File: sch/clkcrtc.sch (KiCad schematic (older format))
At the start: 26 parts, among them Q1 16 MHz, Q2 13.333 MHz

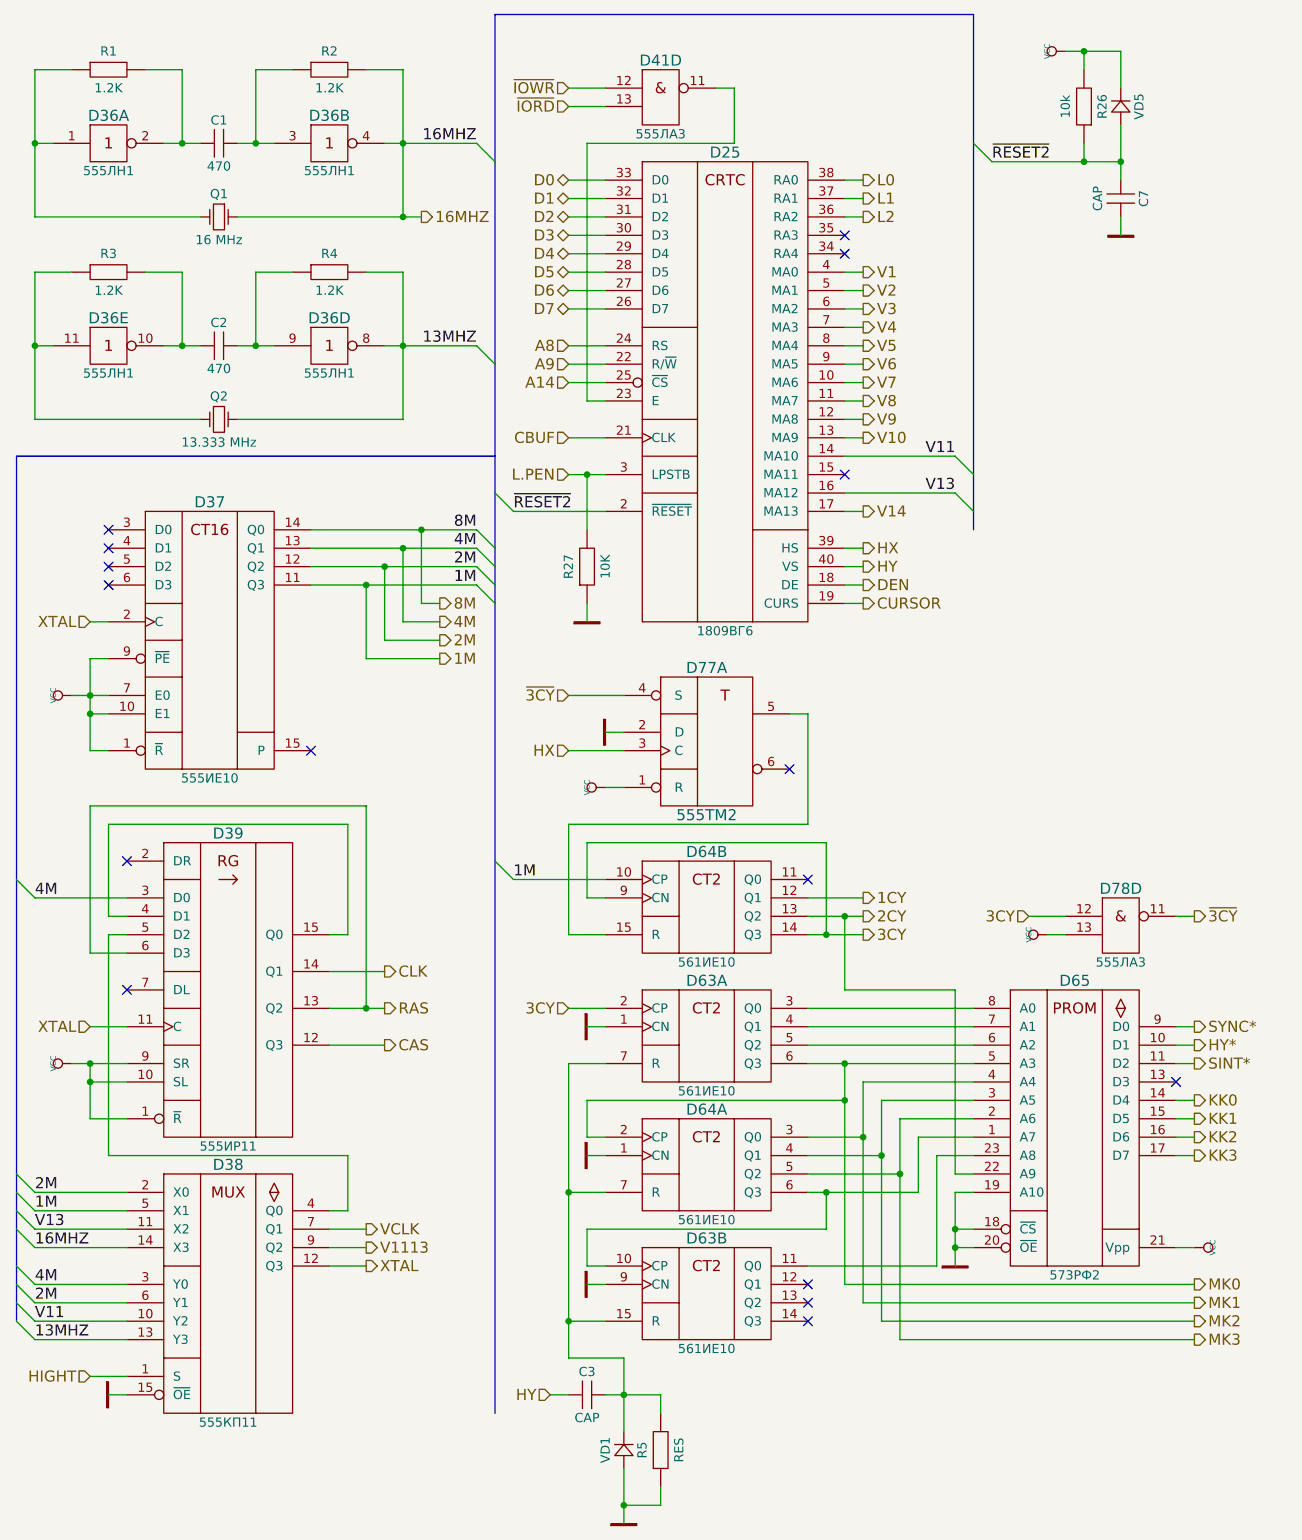
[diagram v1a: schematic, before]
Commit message: IR22 and IR23 symbols updated, part values updated
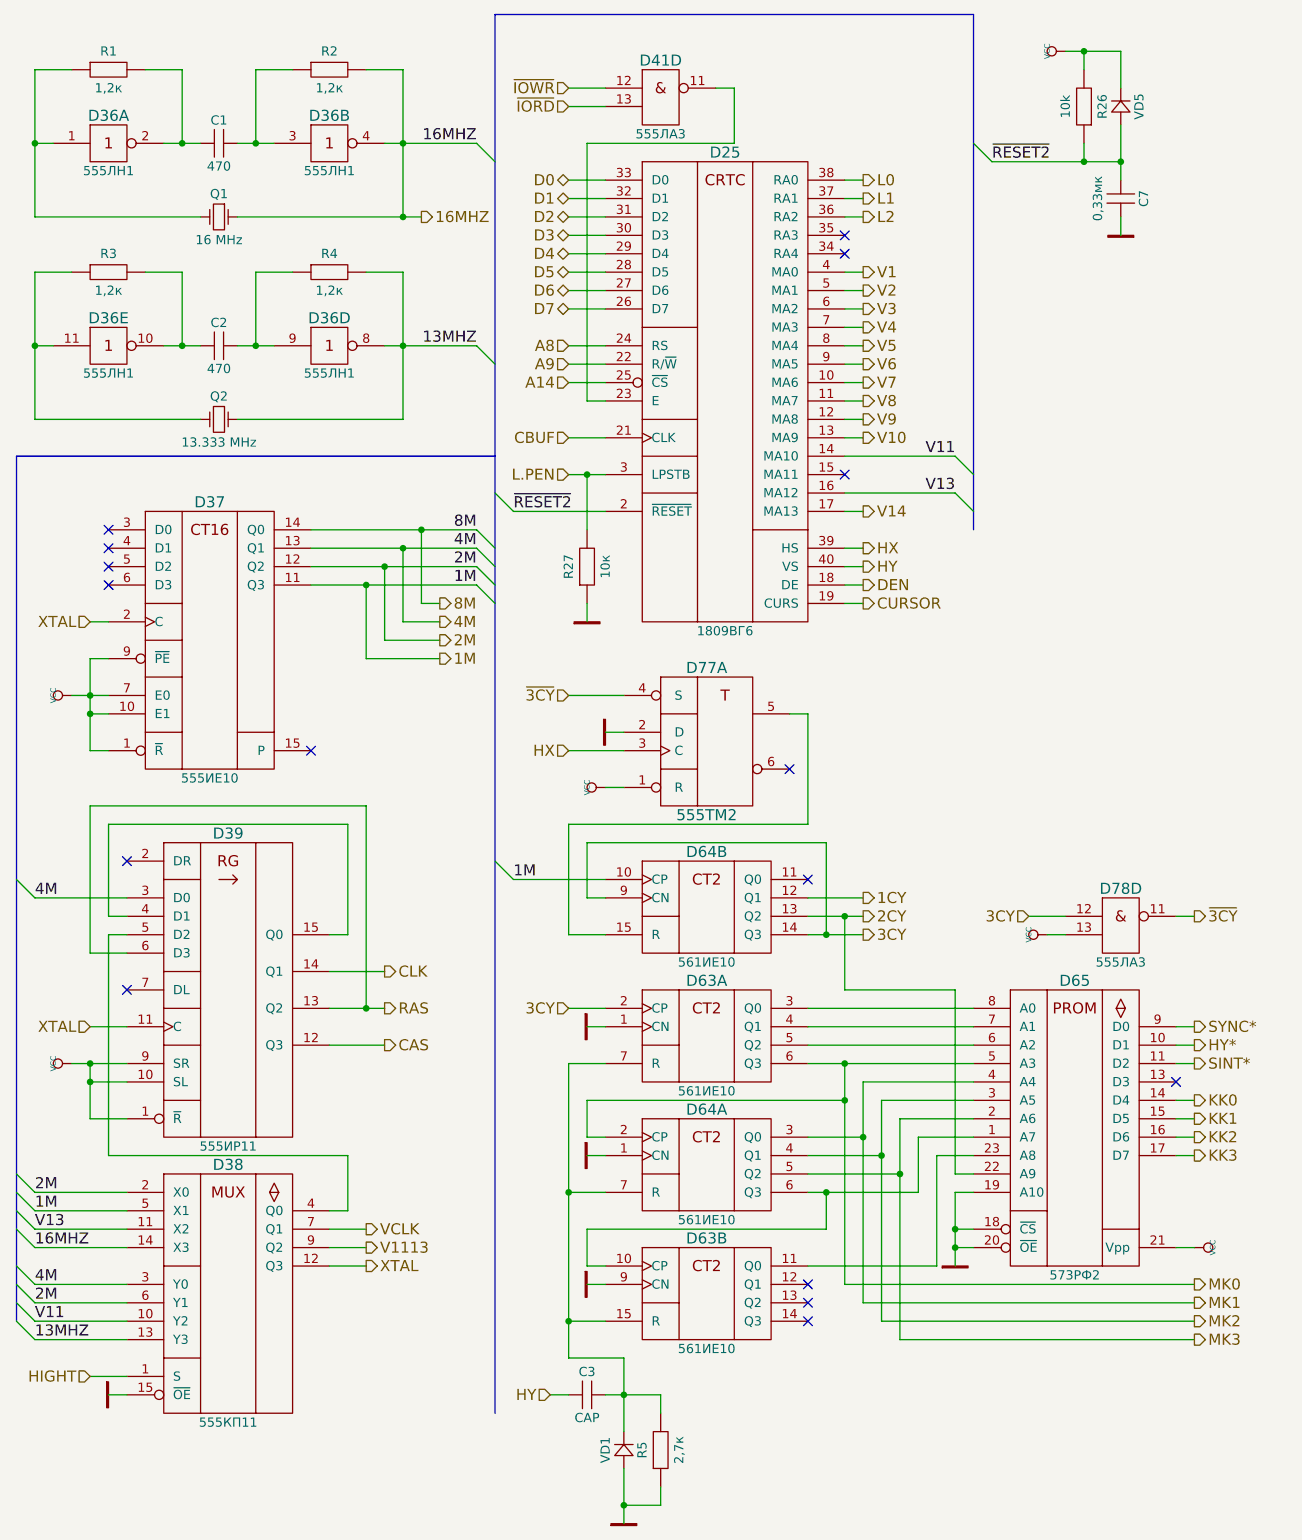
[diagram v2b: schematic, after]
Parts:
- C7: value CAP -> 0,33мк
- R1, R2, R3, R4: value 1.2K -> 1,2к
- R27: value 10K -> 10к
- R5: value RES -> 2,7к
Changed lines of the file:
@@
 P 1300 1100
 F 0 "R1" H 1300 1200 50  0000 C CNN
-F 1 "1.2K" H 1300 1000 50  0000 C CNN
+F 1 "1,2к" H 1300 1000 50  0000 C CNN
 F 2 "MyLib_metric:Resistor_Horizontal_RM7.5mm" H 1300 1050 60  0001 C CNN
 F 3 "" H 1300 1050 60  0000 C CNN
@@
 P 2500 1100
 F 0 "R2" H 2500 1200 50  0000 C CNN
-F 1 "1.2K" H 2500 1000 50  0000 C CNN
+F 1 "1,2к" H 2500 1000 50  0000 C CNN
 F 2 "MyLib_metric:Resistor_Horizontal_RM7.5mm" H 2500 1050 60  0001 C CNN
 F 3 "" H 2500 1050 60  0000 C CNN
@@
 P 1300 2200
 F 0 "R3" H 1300 2300 50  0000 C CNN
-F 1 "1.2K" H 1300 2100 50  0000 C CNN
+F 1 "1,2к" H 1300 2100 50  0000 C CNN
 F 2 "MyLib_metric:Resistor_Horizontal_RM7.5mm" H 1300 2150 60  0001 C CNN
 F 3 "" H 1300 2150 60  0000 C CNN
@@
 P 2500 2200
 F 0 "R4" H 2500 2300 50  0000 C CNN
-F 1 "1.2K" H 2500 2100 50  0000 C CNN
+F 1 "1,2к" H 2500 2100 50  0000 C CNN
 F 2 "MyLib_metric:Resistor_Horizontal_RM7.5mm" H 2500 2150 60  0001 C CNN
 F 3 "" H 2500 2150 60  0000 C CNN
@@
 P 4300 8600
 F 0 "R5" H 4300 8700 50  0000 C CNN
-F 1 "RES" H 4300 8500 50  0000 C CNN
+F 1 "2,7к" H 4300 8500 50  0000 C CNN
 F 2 "MyLib_metric:Resistor_Horizontal_RM7.5mm" H 4300 8550 60  0001 C CNN
 F 3 "" H 4300 8550 60  0000 C CNN
@@
 P 6800 1800
 F 0 "C7" H 6800 1925 50  0000 C CNN
-F 1 "CAP" H 6800 1675 50  0000 C CNN
+F 1 "0,33мк" H 6800 1675 50  0000 C CNN
 F 2 "MyLib_metric:C_Disc_D7.5_P2.5" H 6800 1750 60  0001 C CNN
 F 3 "" H 6800 1750 60  0000 C CNN
@@
 P 3900 3800
 F 0 "R27" H 3900 3900 50  0000 C CNN
-F 1 "10K" H 3900 3700 50  0000 C CNN
+F 1 "10к" H 3900 3700 50  0000 C CNN
 F 2 "MyLib_metric:Resistor_Horizontal_RM7.5mm" H 3900 3750 60  0001 C CNN
 F 3 "" H 3900 3750 60  0000 C CNN

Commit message: C8 on its place
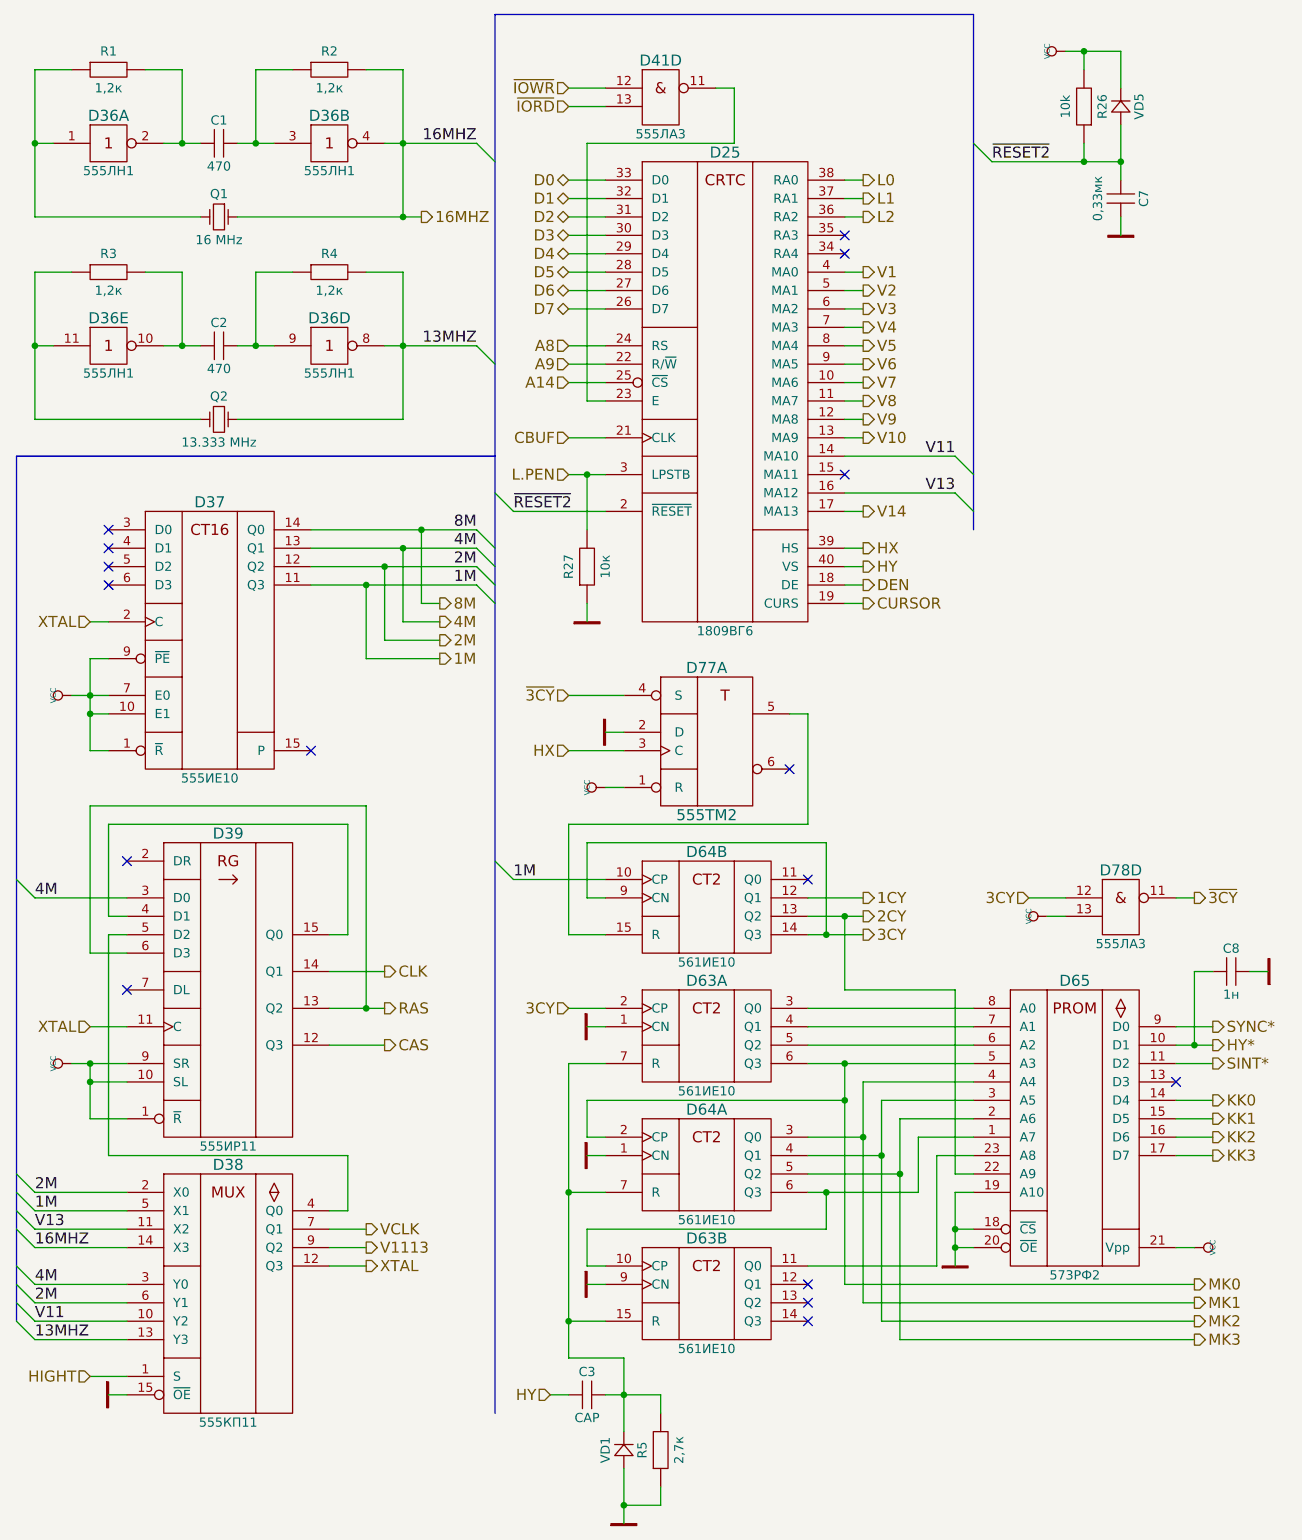
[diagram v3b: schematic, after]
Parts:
- added C8: 1н, MyLib_metric:C_Disc_D7.5_P2.5, symbol CAP
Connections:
- net GND: now also C8.2
- net HY*: now also C8.1
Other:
- moved on the sheet: D78D
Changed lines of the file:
@@
 $EndComp
 NoConn ~ 7100 6600
-Text HLabel 7200 6700 2    60   Output ~ 0
+Text HLabel 7300 6700 2    60   Output ~ 0
 KK0
-Text HLabel 7200 6800 2    60   Output ~ 0
+Text HLabel 7300 6800 2    60   Output ~ 0
 KK1
-Text HLabel 7200 6900 2    60   Output ~ 0
+Text HLabel 7300 6900 2    60   Output ~ 0
 KK2
-Text HLabel 7200 7000 2    60   Output ~ 0
+Text HLabel 7300 7000 2    60   Output ~ 0
 KK3
 Text HLabel 7200 7700 2    60   Output ~ 0
@@
 	1    0    0    -1
 $EndComp
-Text HLabel 7200 6500 2    60   Output ~ 0
+Text HLabel 7300 6500 2    60   Output ~ 0
 SINT*
 $Comp
@@
 L 555ЛА3 D78
 U 4 1 567812C8
-P 6800 5700
-F 0 "D78" H 6800 5850 60  0000 C CNN
-F 1 "555ЛА3" H 6800 5450 50  0000 C CNN
-F 2 "MyLib_metric:DIP-14" H 6800 5650 60  0001 C CNN
-F 3 "" H 6800 5650 60  0000 C CNN
-	4    6800 5700
+P 6800 5600
+F 0 "D78" H 6800 5750 60  0000 C CNN
+F 1 "555ЛА3" H 6800 5350 50  0000 C CNN
+F 2 "MyLib_metric:DIP-14" H 6800 5550 60  0001 C CNN
+F 3 "" H 6800 5550 60  0000 C CNN
+	4    6800 5600
 	1    0    0    -1
 $EndComp
@@
 L VCC #PWR0131
 U 1 1 5678218D
-P 6400 5800
-F 0 "#PWR0131" H 6400 5900 30  0001 C CNN
-F 1 "VCC" H 6400 5900 30  0000 C CNN
-F 2 "" H 6400 5800 60  0000 C CNN
-F 3 "" H 6400 5800 60  0000 C CNN
-	1    6400 5800
+P 6400 5700
+F 0 "#PWR0131" H 6400 5800 30  0001 C CNN
+F 1 "VCC" H 6400 5800 30  0000 C CNN
+F 2 "" H 6400 5700 60  0000 C CNN
+F 3 "" H 6400 5700 60  0000 C CNN
+	1    6400 5700
 	0    -1   -1   0
 $EndComp
 Text HLabel 5400 5800 2    60   Output ~ 0
 3CY
-Text HLabel 7200 5700 2    60   Output ~ 0
+Text HLabel 7200 5600 2    60   Output ~ 0
 ~3CY
 Text HLabel 5400 5600 2    60   Output ~ 0
@@
 Text HLabel 3800 6200 0    60   Input ~ 0
 3CY
-Text HLabel 6300 5700 0    60   Input ~ 0
+Text HLabel 6300 5600 0    60   Input ~ 0
 3CY
 Text HLabel 3100 4000 2    60   Output ~ 0
@@
 	2400 3600 3300 3600
 Wire Wire Line
-	3300 3700 2400 3700
-Wire Wire Line
-	3300 3800 2400 3800
-Wire Wire Line
-	3300 3900 2400 3900
+	2400 3700 3300 3700
+Wire Wire Line
+	2400 3800 3300 3800
+Wire Wire Line
+	2400 3900 3300 3900
 Wire Wire Line
 	900  7200 1400 7200
@@
 	7200 7500 7100 7500
 Wire Wire Line
-	7100 6300 7200 6300
-Wire Wire Line
-	7200 6400 7100 6400
-Wire Wire Line
-	7200 7000 7100 7000
-Wire Wire Line
-	7100 6900 7200 6900
-Wire Wire Line
-	7100 6800 7200 6800
-Wire Wire Line
-	7100 6700 7200 6700
+	7100 6300 7300 6300
+Wire Wire Line
+	7100 6400 7300 6400
+Wire Wire Line
+	7300 7000 7100 7000
+Wire Wire Line
+	7100 6900 7300 6900
+Wire Wire Line
+	7100 6800 7300 6800
+Wire Wire Line
+	7100 6700 7300 6700
 Wire Wire Line
 	5300 7700 7200 7700
@@
 Connection ~ 3800 7900
 Wire Wire Line
-	7100 6500 7200 6500
+	7100 6500 7300 6500
 Wire Wire Line
 	3800 6200 4000 6200
@@
 	1200 8200 1400 8200
 Wire Wire Line
-	6300 5700 6500 5700
-Wire Wire Line
-	7100 5700 7200 5700
-Wire Wire Line
-	6400 5800 6500 5800
+	6300 5600 6500 5600
+Wire Wire Line
+	7100 5600 7200 5600
+Wire Wire Line
+	6400 5700 6500 5700
 Connection ~ 2900 1900
 Wire Wire Line
@@
 Entry Wire Line
 	6000 1500 6100 1600
-Text HLabel 7200 6400 2    60   Output ~ 0
+Text HLabel 7300 6400 2    60   Output ~ 0
 HY*
-Text HLabel 7200 6300 2    60   Output ~ 0
+Text HLabel 7300 6300 2    60   Output ~ 0
 SYNC*
 Text HLabel 3100 4100 2    60   Output ~ 0
@@
 	2700 4300 2700 3900
 Connection ~ 2700 3900
+$Comp
+L CAP C8
+U 1 1 586F6BCD
+P 7400 6000
+F 0 "C8" H 7400 6125 50  0000 C CNN
+F 1 "1н" H 7400 5875 50  0000 C CNN
+F 2 "MyLib_metric:C_Disc_D7.5_P2.5" H 7400 5950 60  0001 C CNN
+F 3 "" H 7400 5950 60  0000 C CNN
+	1    7400 6000
+	1    0    0    -1
+$EndComp
+Wire Wire Line
+	7300 6000 7200 6000
+Wire Wire Line
+	7200 6000 7200 6400
+Connection ~ 7200 6400
+$Comp
+L GND #PWR0136
+U 1 1 586F77A2
+P 7600 6000
+F 0 "#PWR0136" H 7600 6000 30  0001 C CNN
+F 1 "GND" H 7600 5930 30  0001 C CNN
+F 2 "" H 7600 6000 60  0000 C CNN
+F 3 "" H 7600 6000 60  0000 C CNN
+	1    7600 6000
+	0    -1   -1   0
+$EndComp
+Wire Wire Line
+	7600 6000 7500 6000
 $EndSCHEMATC
